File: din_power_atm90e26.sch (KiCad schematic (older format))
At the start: 46 parts, among them J1 CONN_01X06, J2 Conn_02x18_Counter_Clockwise, U1 TRS35_3, U2 TRS35_3, U3 AP7365-33YG-13, U4 Hi-Link_SMPS, U5 dc-dc, U6 AP7365-33YG-13

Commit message: First pass at layout matching meter PCB
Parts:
- removed C2: .033u, Capacitor_SMD:C_0805_2012Metric, symbol device:C
- removed J2: Conn_02x18_Counter_Clockwise, hi-link_smps:PCIE-36-SKT, symbol conn:Conn_02x18_Counter_Clockwise
- removed R14, R17, R24, R7: 220K, Resistors_SMD:R_1206, symbol device:R
- removed R27: 1K, Resistor_SMD:R_0805_2012Metric, symbol device:R
- added J2: CONN_02X18, hi-link_smps:PCIE-36-SKT, symbol din_power_atm90e26-rescue:CONN_02X18
- C4, C5, C6, C7, D1, D2: footprint (none) -> Capacitor_SMD:C_0805_2012Metric
- F1: footprint Capacitors_THT:C_Disc_D10.0mm_W2.5mm_P5.00mm -> Capacitor_THT:C_Disc_D10.5mm_W5.0mm_P5.00mm
- L1: footprint Inductors_SMD:L_1206 -> Inductor_SMD:L_1206_3216Metric
- R12, R13, R15, R16, R22, R23, R5, R6: footprint Resistors_SMD:R_1206 -> Resistor_SMD:R_1206_3216Metric
- U1, U2: footprint (none) -> HappyDayEnergyMonitor:Audio-Jack
- U3, U6: footprint (none) -> Package_TO_SOT_SMD:SOT-89-3
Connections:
- net labels added: 3V3_CPU, 3V3_M, GND_CPU, GND_M, VP_0, VP_1
- net labels removed: +3.3V_ISO, +3V3, UA_SAMP, UB_SAMP, UC_SAMP, uc_1, uc_2, uc_3
- wire segments 106 -> 105
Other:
- note added: "Pin Mappings based on Footprint."

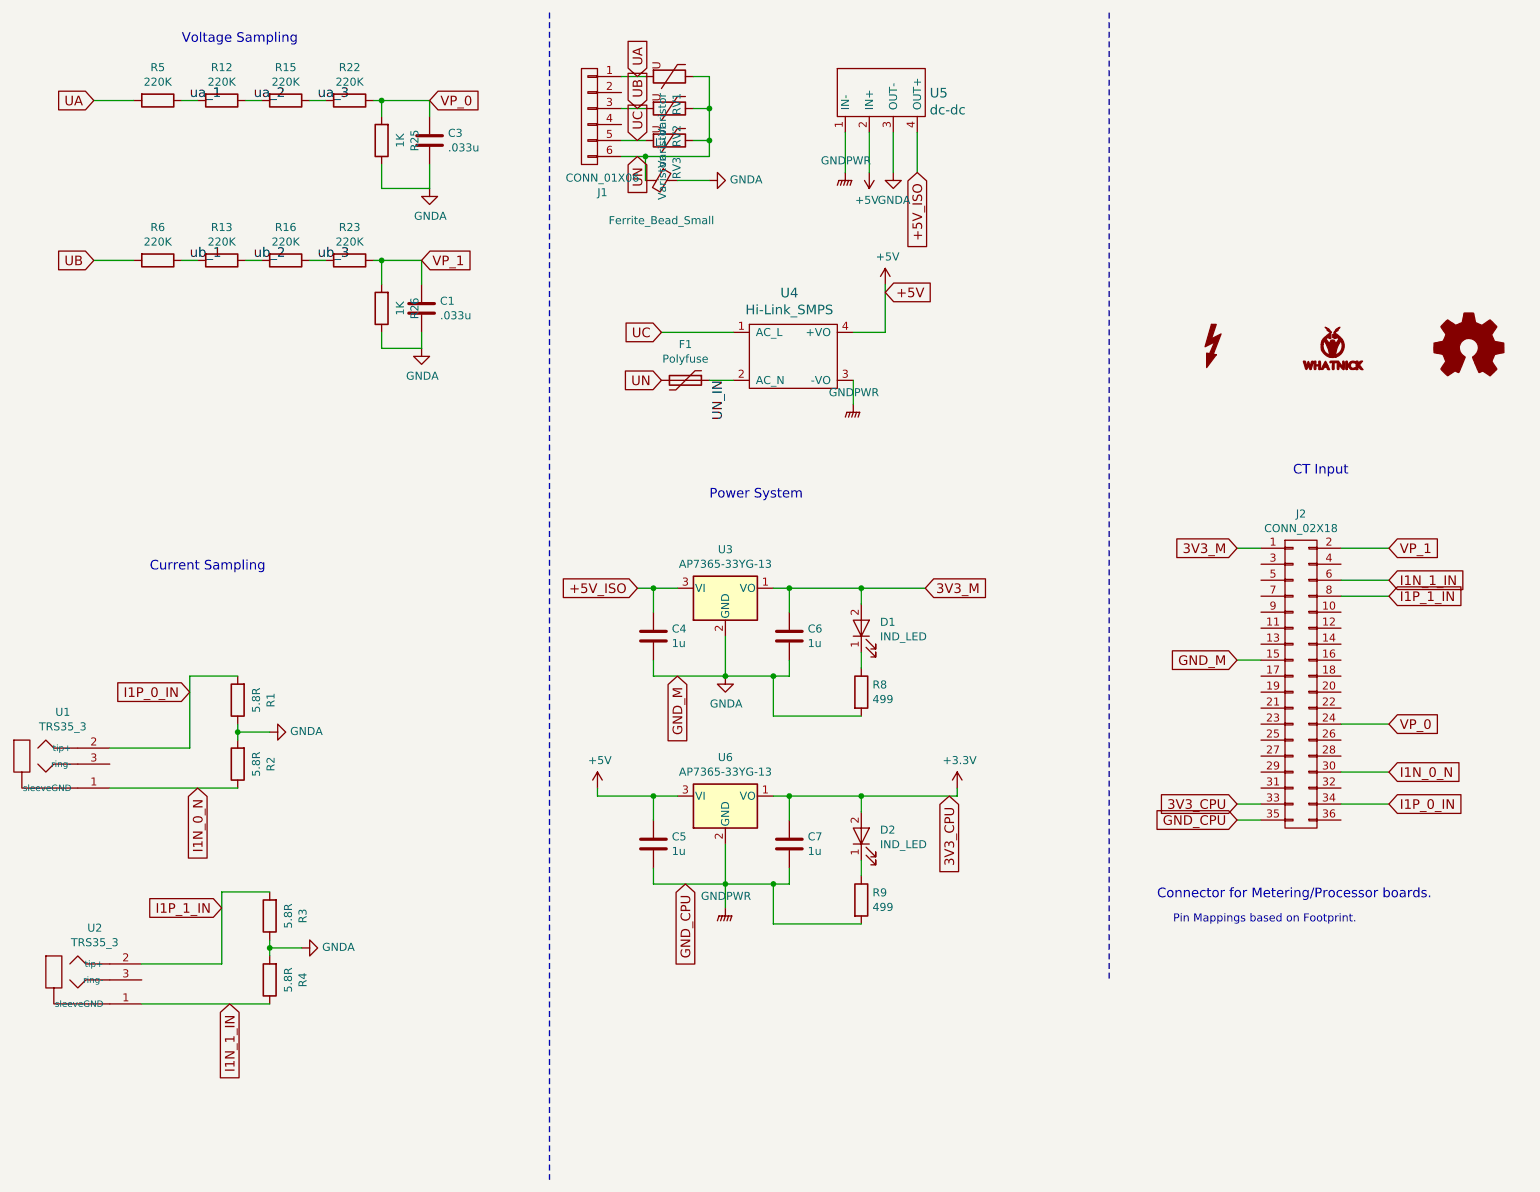
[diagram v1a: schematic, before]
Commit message: Updated PCI Express connector (v. B)
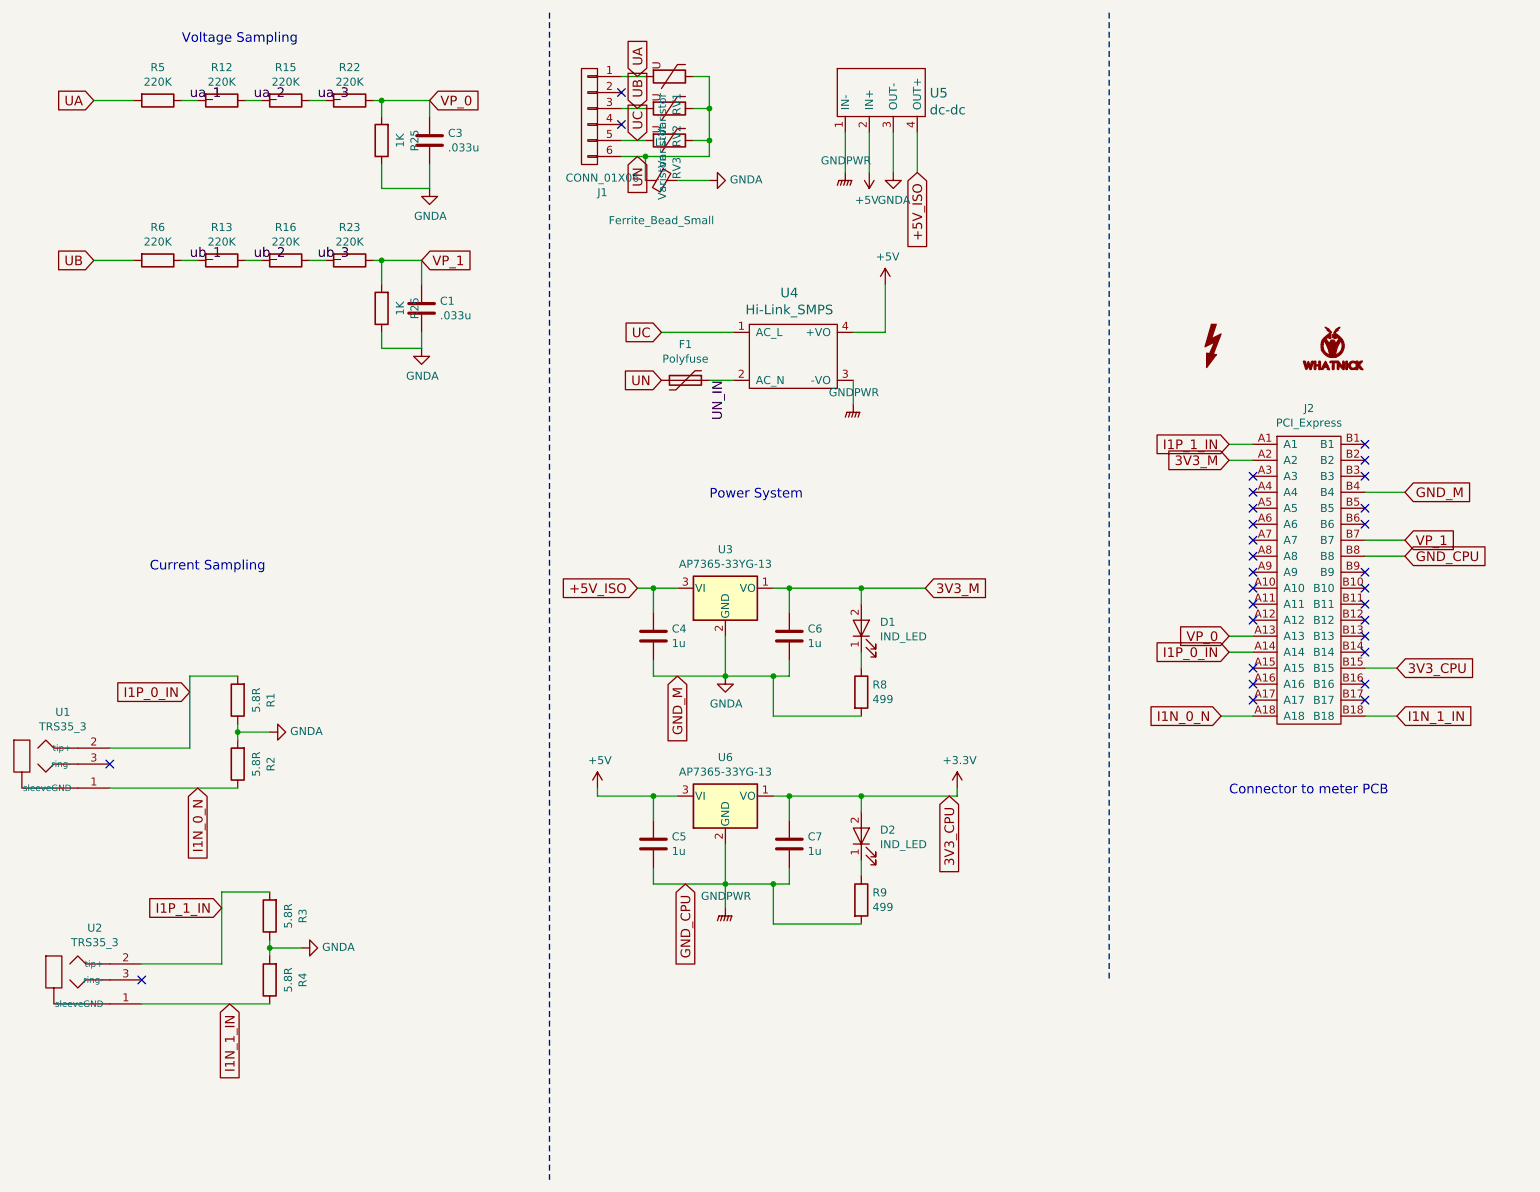
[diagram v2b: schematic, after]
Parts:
- removed J2: CONN_02X18, hi-link_smps:PCIE-36-SKT, symbol din_power_atm90e26-rescue:CONN_02X18
- removed LOGO_OSHW1: Logo_Open_Hardware_Small, Symbols:OSHW-Symbol_6.7x6mm_SilkScreen, symbol graphic_symbols:Logo_Open_Hardware_Small
- added J2: PCI_Express, FitHome_PCI_Express_TH:PCIE-36-SKT, symbol FitHome:PCI_Express
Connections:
- net +3V3: now also J2.B15
- net 3V3_M: now also J2.A2
- net GNDA: now also J2.B4
- net GNDPWR: now also J2.B8
- net I1N_0_N: now also J2.A18
- net I1N_1_IN: now also J2.B18
- net I1P_0_IN: now also J2.A14
- net I1P_1_IN: now also J2.A1
- net VP_0: now also J2.A13
- net VP_1: now also J2.B7
- no-connect marks 0 -> 30
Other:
- note added: "Connector to meter PCB"
- note removed: "CT Input"
- note removed: "Connector for Metering/Processor boards."
- note removed: "Pin Mappings based on Footprint."
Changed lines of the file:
@@
 Text Notes 1600 4000 0    60   ~ 0
 Current Sampling
-Text Notes 8750 3400 0    60   ~ 0
-CT Input
-Text Notes 7900 6050 0    60   ~ 0
-Connector for Metering/Processor boards.
+Text Notes 8350 5400 0    60   ~ 0
+Connector to meter PCB
 Text GLabel 1900 5350 3    60   Input ~ 0
 I1N_0_N
@@
 Text GLabel 3300 2050 2    60   Input ~ 0
 VP_1
-Text GLabel 9350 4950 2    60   Input ~ 0
+Text GLabel 8350 4400 0    60   Input ~ 0
 VP_0
-Text GLabel 9350 3850 2    60   Input ~ 0
+Text GLabel 9450 3800 2    60   Input ~ 0
 VP_1
-Text GLabel 8400 4550 0    60   Input ~ 0
+Text GLabel 9450 3500 2    60   Input ~ 0
 GND_M
-Text GLabel 8400 3850 0    60   Input ~ 0
+Text GLabel 8350 3300 0    60   Input ~ 0
 3V3_M
-Text GLabel 8400 5550 0    60   Input ~ 0
+Text GLabel 9450 3900 2    60   Input ~ 0
 GND_CPU
-Text GLabel 8400 5450 0    60   Input ~ 0
+Text GLabel 9400 4600 2    60   Input ~ 0
 3V3_CPU
 Text Label 5200 2800 3    60   ~ 0
@@
 	1    0    0    -1
 $EndComp
-Text GLabel 6200 2250 2    60   Input ~ 0
-+5V
 $Comp
 L whatnick:LOGO G1
@@
 F 5 "1" H 9000 2600 60  0001 C CNN "DNP"
 	1    9000 2600
-	1    0    0    -1
-$EndComp
-$Comp
-L graphic_symbols:Logo_Open_Hardware_Small LOGO_OSHW1
-U 1 1 5A0F959B
-P 9850 2600
-F 0 "LOGO_OSHW1" H 9850 2875 50  0001 C CNN
-F 1 "Logo_Open_Hardware_Small" H 9850 2375 50  0001 C CNN
-F 2 "Symbols:OSHW-Symbol_6.7x6mm_SilkScreen" H 9850 2600 50  0001 C CNN
-F 3 "" H 9850 2600 50  0001 C CNN
-F 4 "X" H 9850 2600 50  0001 C CNN "PN"
-F 5 "1" H 9850 2600 60  0001 C CNN "DNP"
-	1    9850 2600
 	1    0    0    -1
 $EndComp
@@
 Wire Notes Line
 	7600 500  7600 6550
-Text GLabel 9350 5450 2    60   Input ~ 0
+Text GLabel 8350 4500 0    60   Input ~ 0
 I1P_0_IN
-Text GLabel 9350 5250 2    60   Input ~ 0
+Text GLabel 8300 4900 0    60   Input ~ 0
 I1N_0_N
-Text GLabel 9350 4150 2    60   Input ~ 0
+Text GLabel 8350 3200 0    60   Input ~ 0
 I1P_1_IN
-Text GLabel 9350 4050 2    60   Input ~ 0
+Text GLabel 9400 4900 2    60   Input ~ 0
 I1N_1_IN
 Text GLabel 4900 4650 3    60   Input ~ 0
@@
 Text GLabel 4950 5950 3    60   Input ~ 0
 GND_CPU
-Text Notes 8000 6200 0    50   ~ 0
-Pin Mappings based on Footprint.
-Wire Wire Line
-	8400 3850 8550 3850
-Wire Wire Line
-	8550 4550 8400 4550
-Wire Wire Line
-	8400 5450 8550 5450
-Wire Wire Line
-	8550 5550 8400 5550
-Wire Wire Line
-	9350 5450 9050 5450
-Wire Wire Line
-	9350 5250 9050 5250
-Wire Wire Line
-	9350 4950 9050 4950
-Wire Wire Line
-	9350 4150 9050 4150
-Wire Wire Line
-	9350 4050 9050 4050
-Wire Wire Line
-	9350 3850 9050 3850
-$Comp
-L din_power_atm90e26-rescue:CONN_02X18 J2
-U 1 1 5C996796
-P 8800 4700
-F 0 "J2" H 8800 5765 50  0000 C CNN
-F 1 "CONN_02X18" H 8800 5674 50  0000 C CNN
-F 2 "hi-link_smps:PCIE-36-SKT" H 8800 3650 50  0001 C CNN
-F 3 "" H 8800 3650 50  0001 C CNN
-	1    8800 4700
-	1    0    0    -1
-$EndComp
+Wire Wire Line
+	8350 3300 8500 3300
+Wire Wire Line
+	9400 4900 9200 4900
+Wire Wire Line
+	9450 3800 9200 3800
+$Comp
+L FitHome:PCI_Express J2
+U 1 1 5CA81E0B
+P 8750 4700
+F 0 "J2" H 8850 6425 50  0000 C CNN
+F 1 "PCI_Express" H 8850 6334 50  0000 C CNN
+F 2 "FitHome_PCI_Express_TH:PCIE-36-SKT" H 8750 4700 50  0001 C CNN
+F 3 "" H 8750 4700 50  0001 C CNN
+	1    8750 4700
+	1    0    0    -1
+$EndComp
+Wire Wire Line
+	9400 4600 9200 4600
+Wire Wire Line
+	8350 4500 8500 4500
+Wire Wire Line
+	8500 4900 8300 4900
+NoConn ~ 8500 4800
+NoConn ~ 8500 4700
+NoConn ~ 8500 4600
+NoConn ~ 8500 4300
+NoConn ~ 9200 4800
+NoConn ~ 9200 4700
+NoConn ~ 9200 4500
+NoConn ~ 9200 4400
+NoConn ~ 9200 4300
+Wire Wire Line
+	9450 3900 9200 3900
+Wire Wire Line
+	9450 3500 9200 3500
+NoConn ~ 9200 3200
+NoConn ~ 9200 3300
+NoConn ~ 9200 3400
+NoConn ~ 9200 3600
+NoConn ~ 9200 3700
+NoConn ~ 9200 4000
+NoConn ~ 9200 4100
+NoConn ~ 9200 4200
+Wire Wire Line
+	8500 3200 8350 3200
+NoConn ~ 8500 3400
+NoConn ~ 8500 3500
+NoConn ~ 8500 3600
+NoConn ~ 8500 3700
+NoConn ~ 8500 3800
+NoConn ~ 8500 3900
+NoConn ~ 8500 4000
+Wire Wire Line
+	8500 4400 8350 4400
+NoConn ~ 8500 4100
+NoConn ~ 8500 4200
+NoConn ~ 4550 1000
+NoConn ~ 4550 1200
+NoConn ~ 1350 5200
+NoConn ~ 1550 6550
 $EndSCHEMATC

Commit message: Evolved readme.
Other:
- note added: "120VAC -> 5 and 3.3VDC"
- note added: "Incoming 120V"
- note removed: "Power System"
- moved on the sheet: C4, C5, C6, C7, D1, D2, F1, J1, L1, R8, R9, RV1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

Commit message: updated readme
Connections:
- net +3V3: now also J2.B17; no longer J2.B15
- net 3V3_M: now also J2.B2; no longer J2.A2
- net GNDPWR: now also J2.B16; no longer J2.B8
- net I1N_0_N: now also J2.A16; no longer J2.A18
- net I1N_1_IN: now also J2.A4; no longer J2.B18
- net I1P_0_IN: now also J2.A17; no longer J2.A14
- net I1P_1_IN: now also J2.A8; no longer J2.A1
- net VP_0: now also J2.B12; no longer J2.A13
- net VP_1: now also J2.B6; no longer J2.B7
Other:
- moved on the sheet: R1, R2, R3, R4, U1, U2

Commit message: updated schematic after changing dir name.
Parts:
- J2: symbol FitHome:PCI_Express -> din_power_atm90e26-rescue:PCI_Express-FitHome
- U1, U2: symbol Fithome:TRS35_3 -> din_power_atm90e26-rescue:TRS35_3-Fithome
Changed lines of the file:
@@
 	6100 4750 6100 4850
 $Comp
-L Fithome:TRS35_3 U1
+L din_power_atm90e26-rescue:TRS35_3-Fithome U1
 U 1 1 5C8F08EE
 P 1050 4900
@@
 	2100 4400 2100 4850
 $Comp
-L Fithome:TRS35_3 U2
+L din_power_atm90e26-rescue:TRS35_3-Fithome U2
 U 1 1 5C8FFEC9
 P 1250 6250
@@
 	9450 3700 9200 3700
 $Comp
-L FitHome:PCI_Express J2
+L din_power_atm90e26-rescue:PCI_Express-FitHome J2
 U 1 1 5CA81E0B
 P 8750 4700

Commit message: Updates as build Power PCB Rev B.
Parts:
- J1: footprint Connectors_Phoenix:PhoenixContact_MC-G_06x5.08mm_Angled -> HappyDayEnergyMonitor:PhoenixContact_MC-G_06x5.08mm_Angled
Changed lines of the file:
@@
 F 0 "J1" H 4700 700 50  0000 C CNN
 F 1 "CONN_01X06" V 4800 1200 50  0000 C CNN
-F 2 "Connectors_Phoenix:PhoenixContact_MC-G_06x5.08mm_Angled" H 3450 -300 50  0001 C CNN
+F 2 "HappyDayEnergyMonitor:PhoenixContact_MC-G_06x5.08mm_Angled" H 3450 -300 50  0001 C CNN
 F 3 "" H 3450 -300 50  0001 C CNN
 F 4 "1759059" H 4650 1200 50  0001 C CNN "PN"
